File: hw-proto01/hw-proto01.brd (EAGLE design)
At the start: 100 x 80 mm, 4 parts, among them Q1 PMOS, Q2 PMOS

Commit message: initial eagle drawings
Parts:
- removed R1, R2: (no value), rcl:R0805
- added CAN: (no value), con-amp-quick:03P
- added IC1, IC2: VN5E160MSTR-E, VN5E160MSTR-E:SOIC127P600X175-8N
- added IC3: MCP2562T-H_SN, MCP2562T-H_SN:SOIC127P600X175-8N
- added IC4: ESP32-WROOM-32E-N8R2, ESP32-WROOM-32E-N8R2:ESP32WROOM32EN8R2
- added PWR: 4DB-P108-06, 4DB-P108-06:4DBP10806
- moved Q1 44.4 mm to (21.6, 55.9)
- moved Q2 44.4 mm to (58.4, 55.9)
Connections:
- new net GND: IC1.1, IC2.1, IC3.3, IC4.1, IC4.15, IC4.38, IC4.39, IC4.40, IC4.41, IC4.42, IC4.43, IC4.44, IC4.45, IC4.46, IC4.47, PWR.2, PWR.4, PWR.6
- new net N$1: CAN.1, IC3.7
- new net N$2: CAN.3, IC3.6
- new net SW1: PWR.3, Q1.3
- new net SW2: PWR.5, Q2.3
- net GATE1D: now also IC1.6, IC1.7; no longer R1.1
- net GATE2D: now also IC2.6, IC2.7; no longer R2.1
- net VPP: now also PWR.1; no longer R1.2, R2.2

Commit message: initial drawings
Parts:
- added PS1: TSR_1-2433E, TSR_1-2433E:TSR-1-2433
- moved PWR 86.4 mm to (6.35, 67.3)
- moved CAN 57.5 mm to (8.89, 24.1)
- moved IC4 56.9 mm to (29.2, 27.9), turned to 180 degrees
- moved IC3 43.5 mm to (8.89, 39.4)
- moved Q2 16.7 mm to (41.9, 58.4), turned to 180 degrees
- moved IC1 14.5 mm to (25.4, 47.0)
- moved IC2 8.52 mm to (41.9, 47.0)
- moved Q1 4.58 mm to (25.4, 58.4), turned to 180 degrees
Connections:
- new net +3V3: IC3.2, IC4.2, PS1.3
- net GND: now also PS1.2
- net VPP: now also PS1.1
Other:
- board size 100 x 80 mm -> 54.3 x 59.7 mm

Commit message: initial layout and routing
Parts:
- removed IC4: ESP32-WROOM-32E-N8R2, ESP32-WROOM-32E-N8R2:ESP32WROOM32EN8R2
- removed PS1: TSR_1-2433E, TSR_1-2433E:TSR-1-2433
- added C1, C2: 100n, rcl:C0603K
- added IC5: IR4427S, ir:SO08
- added J1, J2: 000, rcl:0207/12
- added MCU: ESP32-WROOM-32E, ESP32-WROOM-32E-N8R2:ESP32WROOM32EN8R2
- added R1, R2: 10K0, rcl:0204/7
- added VREG1: +5V, TSR_1-2433E:TSR-1-2433
- added VREG2: +3V3, TSR_1-2433E:TSR-1-2433
- CAN: device con-amp-quick:03P -> con-wago-500:W237-103
- moved IC1 17.6 mm to (40.6, 55.9), turned to 90 degrees
- moved IC2 10.9 mm to (48.3, 55.9), turned to 90 degrees
- moved Q2 10.2 mm to (31.8, 57.1)
- moved IC3 7.41 mm to (12.7, 33.0), turned to 180 degrees
- moved Q1 2.84 mm to (22.9, 57.1)
- moved CAN 1.27 mm to (8.89, 25.4)
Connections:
- removed net GATE1D: IC1.6, IC1.7, Q1.1
- removed net GATE2D: IC2.6, IC2.7, Q2.1
- removed net VPP: PS1.1, PWR.1, Q1.4, Q2.4
- new net +12V: IC1.5, IC1.8, IC2.5, IC2.8, IC5.6, PWR.1, Q1.4, Q2.4, VREG1.1, VREG2.1
- new net +5V: C1.1, IC3.3, VREG1.3
- new net CAN_RX: IC3.4, MCU.33
- new net CAN_TX: IC3.1, MCU.36
- new net CTL1: IC5.2, MCU.27
- new net CTL2: IC5.4, MCU.28
- new net CTL3: MCU.14, R1.1
- new net CTL4: MCU.13, R2.1
- new net N$3: IC5.5, J2.1
- new net N$4: IC5.7, J1.1
- new net N$5: J1.2, Q1.1
- new net N$6: J2.2, Q2.1
- new net N$7: IC1.2, R1.2
- new net N$8: IC2.2, R2.2
- new net SW3: IC1.6, IC1.7, PWR.5
- new net SW4: IC2.6, IC2.7, PWR.6
- net +3V3: now also C2.1, IC3.5, MCU.2, VREG2.3; no longer IC3.2, IC4.2, PS1.3
- net GND: now also C1.2, C2.2, IC3.2, IC5.3, MCU.1, MCU.15, MCU.38, MCU.39, MCU.40, MCU.41, MCU.42, MCU.43, MCU.44, MCU.45, MCU.46, MCU.47, VREG1.2, VREG2.2; no longer IC3.3, IC4.1, IC4.15, IC4.38, IC4.39, IC4.40, IC4.41, IC4.42, IC4.43, IC4.44, IC4.45, IC4.46, IC4.47, PS1.2, PWR.4, PWR.6
- net N$1: now also CAN.3; no longer CAN.1
- net N$2: now also CAN.1; no longer CAN.3
- net SW2: now also PWR.4; no longer PWR.5
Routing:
- net +3V3: track 0.00 -> 63.4 mm, vias 0 -> 2
- net CTL1: track 0.00 -> 16.2 mm
- net N$2: track 0.00 -> 15.0 mm
- net CTL2: track 0.00 -> 14.9 mm
- net CAN_RX: track 0.00 -> 13.7 mm
- net CAN_TX: track 0.00 -> 13.4 mm
- net N$3: track 0.00 -> 13.0 mm
- net +5V: track 0.00 -> 12.0 mm
- net N$1: track 0.00 -> 11.1 mm
- net +12V: track 0.00 -> 9.94 mm, vias 0 -> 34
- net N$7: track 0.00 -> 9.14 mm, vias 0 -> 1
- net CTL4: track 0.00 -> 9.00 mm
- net GND: track 0.00 -> 6.83 mm, vias 0 -> 8
- net N$8: track 0.00 -> 5.06 mm
- net CTL3: track 0.00 -> 4.92 mm
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- added copper zone on layer 1, net +12V
- added copper zone on layer 16, net +12V
- added copper zone on layer 1, net GND
- added copper zone on layer 16, net GND
- added copper zone on layer 1, net SW1
- added copper zone on layer 16, net SW1
- added copper zone on layer 1, net SW2
- added copper zone on layer 16, net SW2
- added copper zone on layer 1, net SW3
- added copper zone on layer 16, net SW3
- added copper zone on layer 1, net SW4
- added copper zone on layer 16, net SW4

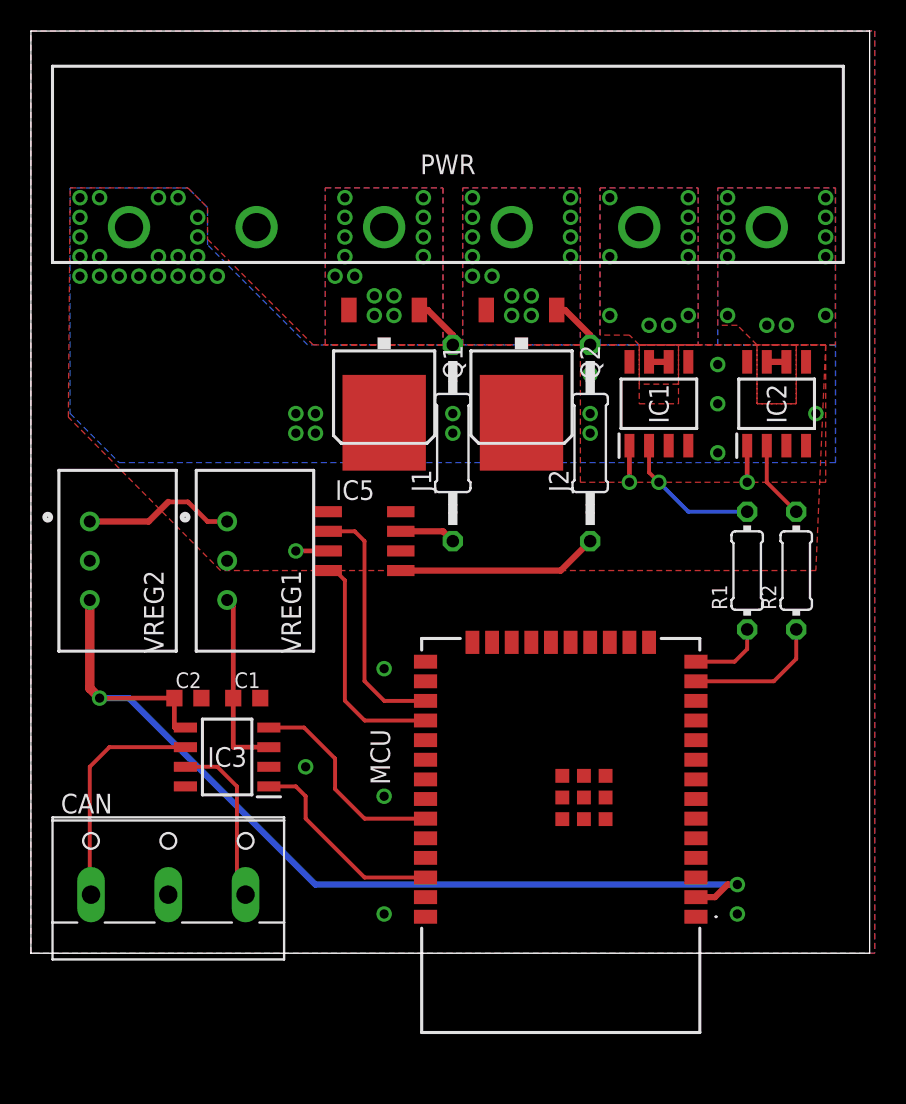
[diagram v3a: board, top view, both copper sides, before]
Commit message: layout refinement, adding passives
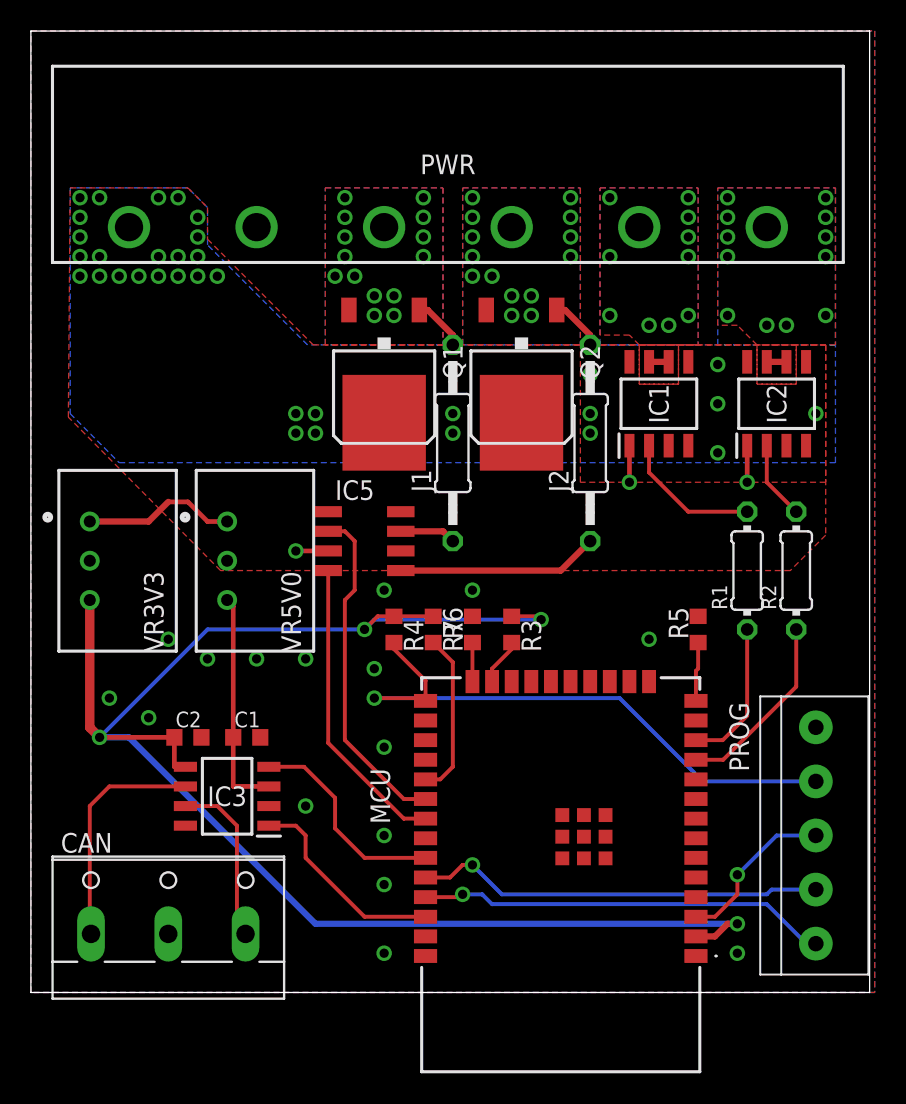
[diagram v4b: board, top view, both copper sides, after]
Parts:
- added PROG: 1X5, adafruit:1X05-3.5MM
- added R3, R4, R5, R6, R7: 47K0, rcl:R0603
- IC1, IC2: value VN5E160MSTR-E -> (none)
- IC3: value MCP2562T-H_SN -> MCP2562T
- PWR: value 4DB-P108-06 -> (none)
- moved IC3 2.54 mm to (12.7, 30.5)
- moved MCU 2.54 mm to (34.3, 25.4)
- moved C1 2.54 mm to (14.0, 34.3)
- moved C2 2.54 mm to (10.2, 34.3)
- moved CAN 2.54 mm to (8.89, 22.9)
- renumbered VREG1 to VR5V0, VREG2 to VR3V3
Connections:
- new net EN: MCU.3, PROG.3
- new net GPIO0: MCU.25, PROG.4, R4.2
- new net GPIO12: MCU.14, R5.1
- new net GPIO15: MCU.23, R3.2
- new net GPIO2: MCU.24, R6.1
- new net GPIO5: MCU.29, R7.2
- new net RXD0: MCU.34, PROG.2
- new net TXD0: MCU.35, PROG.1
- net +3V3: now also R3.1, R4.1, R7.1
- net CTL1: now also MCU.30; no longer MCU.27
- net CTL2: now also MCU.31; no longer MCU.28
- net CTL3: now also MCU.12; no longer MCU.14
- net CTL4: now also MCU.11; no longer MCU.13
- net GND: now also PROG.5, R5.2, R6.2
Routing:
- net +3V3: track 63.4 -> 104.6 mm, vias 2 -> 4
- net GPIO0: track 0.00 -> 38.9 mm, vias 0 -> 1
- net TXD0: track 0.00 -> 26.7 mm, vias 0 -> 1
- net RXD0: track 0.00 -> 26.5 mm, vias 0 -> 1
- net EN: track 0.00 -> 10.7 mm, vias 0 -> 1
- net GPIO5: track 0.00 -> 10.7 mm
- net CTL1: track 16.2 -> 21.9 mm
- net CTL2: track 14.9 -> 19.9 mm
- net CTL3: track 4.92 -> 9.55 mm
- net GPIO12: track 0.00 -> 3.83 mm
- net CTL4: track 9.00 -> 12.2 mm
- net GPIO15: track 0.00 -> 3.05 mm
- net +5V: track 12.0 -> 14.5 mm
- net GPIO2: track 0.00 -> 2.52 mm
- net N$7: vias 1 -> 0
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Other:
- board size 54.3 x 59.7 mm -> 54.3 x 62.2 mm
